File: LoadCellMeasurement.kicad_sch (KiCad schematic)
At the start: 0 parts

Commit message: Add valve control
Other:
- company: (none) -> Queen's Rocket Engineering Team
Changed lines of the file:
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@@
 	(generator_version "9.0")
 	(paper "A4")
+	(title_block
+		(rev "0.1.0")
+		(company "Queen's Rocket Engineering Team")
+	)
 )

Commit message: Add SAFE +24V
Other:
- title: (none) -> Load Cell Measurement
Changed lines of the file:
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@@
 	(paper "A4")
 	(title_block
+		(title "Load Cell Measurement")
 		(rev "0.1.0")
 		(company "Queen's Rocket Engineering Team")

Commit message: Add load cell inputs
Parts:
- added J3: 4-Pin Load Cell, symbol Connector_Generic:Conn_01x04
- added J4: 5-Pin Load Cell, symbol Connector_Generic:Conn_01x05
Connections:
- new net +10V: J4.1 (Pin_1)
- new net +5V: J3.1 (Pin_1)
- new net GND: J3.4 (Pin_4), J4.4 (Pin_4), J4.5 (Pin_5)
- new net LC_FILL_+: J3.2 (Pin_2)
- new net LC_FILL_-: J3.3 (Pin_3)
- new net LC_THRUST_+: J4.2 (Pin_2)
- new net LC_THRUST_-: J4.3 (Pin_3)
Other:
- note added: "Currently this takes up 2 ADC channels per load cell. We could convert this into a single ended reading in the future."

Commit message: v0.1 sch. Add devkit c1 footprint
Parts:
- J3: footprint (none) -> Connector_JST:JST_XH_B4B-XH-A_1x04_P2.50mm_Vertical
- J4: footprint (none) -> Connector_JST:JST_XH_B5B-XH-A_1x05_P2.50mm_Vertical
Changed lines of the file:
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@@
 			)
 		)
-		(property "Footprint" ""
+		(property "Footprint" "Connector_JST:JST_XH_B4B-XH-A_1x04_P2.50mm_Vertical"
 			(at 111.76 85.09 0)
 			(effects
@@
 			)
 		)
-		(property "Footprint" ""
+		(property "Footprint" "Connector_JST:JST_XH_B5B-XH-A_1x05_P2.50mm_Vertical"
 			(at 182.88 87.63 0)
 			(effects

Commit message: routing broken
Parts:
- renumbered J3 to J19, J4 to J20
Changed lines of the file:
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@@
 		(dnp no)
 		(fields_autoplaced yes)
-		(property "Reference" "J3"
+		(property "Reference" "J19"
 			(at 114.3 85.0899 0)
 			(effects
@@
 			(project ""
 				(path "/226c5870-4123-4efa-a2b3-b42d02f59bb7/5c3abfb7-eebf-4fa0-8883-27f893278ab8"
-					(reference "J3")
+					(reference "J19")
 					(unit 1)
 				)
@@
 		(on_board yes)
 		(dnp no)
-		(property "Reference" "#PWR099"
+		(property "Reference" "#PWR095"
 			(at 102.87 97.79 0)
 			(effects
@@
 			(project "nexus"
 				(path "/226c5870-4123-4efa-a2b3-b42d02f59bb7/5c3abfb7-eebf-4fa0-8883-27f893278ab8"
-					(reference "#PWR099")
+					(reference "#PWR095")
 					(unit 1)
 				)
@@
 		(dnp no)
 		(fields_autoplaced yes)
-		(property "Reference" "#PWR098"
+		(property "Reference" "#PWR094"
 			(at 102.87 81.28 0)
 			(effects
@@
 			(project ""
 				(path "/226c5870-4123-4efa-a2b3-b42d02f59bb7/5c3abfb7-eebf-4fa0-8883-27f893278ab8"
-					(reference "#PWR098")
+					(reference "#PWR094")
 					(unit 1)
 				)
@@
 		(on_board yes)
 		(dnp no)
-		(property "Reference" "#PWR096"
+		(property "Reference" "#PWR097"
 			(at 170.18 101.6 0)
 			(effects
@@
 			(project "nexus"
 				(path "/226c5870-4123-4efa-a2b3-b42d02f59bb7/5c3abfb7-eebf-4fa0-8883-27f893278ab8"
-					(reference "#PWR096")
+					(reference "#PWR097")
 					(unit 1)
 				)
@@
 		(dnp no)
 		(fields_autoplaced yes)
-		(property "Reference" "J4"
+		(property "Reference" "J20"
 			(at 185.42 86.3599 0)
 			(effects
@@
 			(project ""
 				(path "/226c5870-4123-4efa-a2b3-b42d02f59bb7/5c3abfb7-eebf-4fa0-8883-27f893278ab8"
-					(reference "J4")
+					(reference "J20")
 					(unit 1)
 				)
@@
 		(dnp no)
 		(fields_autoplaced yes)
-		(property "Reference" "#PWR097"
+		(property "Reference" "#PWR096"
 			(at 170.18 81.28 0)
 			(effects
@@
 			(project ""
 				(path "/226c5870-4123-4efa-a2b3-b42d02f59bb7/5c3abfb7-eebf-4fa0-8883-27f893278ab8"
-					(reference "#PWR097")
-					(unit 1)
-				)
+					(reference "#PWR096")
+					(unit 1)
+				)

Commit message: Fix silk screening
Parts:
- J19, J20: now left out of the parts list
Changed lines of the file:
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@@
 	(title_block
 		(title "Load Cell Measurement")
-		(rev "0.1.0")
+		(rev "1.0.0")
 		(company "Queen's Rocket Engineering Team")
 	)
@@
 		(unit 1)
 		(exclude_from_sim no)
-		(in_bom yes)
+		(in_bom no)
 		(on_board yes)
 		(dnp no)
@@
 		(unit 1)
 		(exclude_from_sim no)
-		(in_bom yes)
+		(in_bom no)
 		(on_board yes)
 		(dnp no)

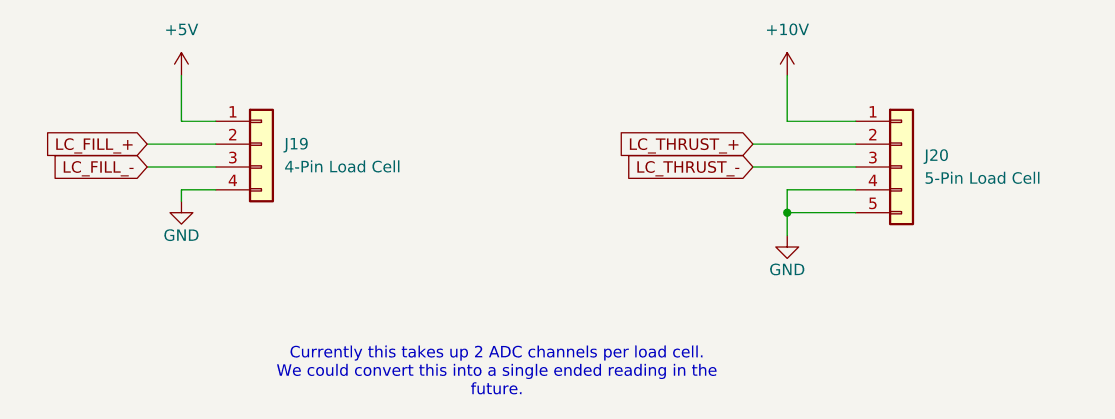
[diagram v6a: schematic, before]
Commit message: Update thrust LC to take +5V. Remove +10V rail
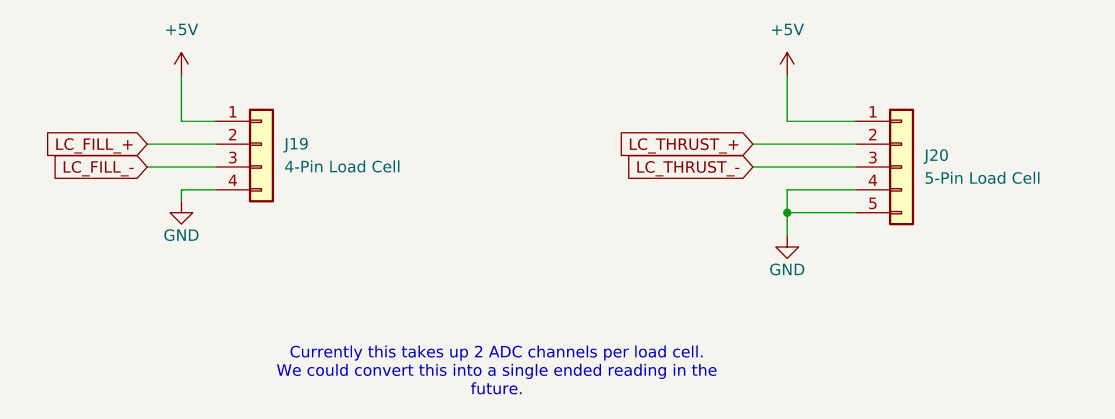
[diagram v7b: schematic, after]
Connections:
- net +10V is gone; now on net +5V: J20.1 (Pin_1)
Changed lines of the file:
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@@
 	)
 	(symbol
-		(lib_id "power:+10V")
+		(lib_id "power:+5V")
 		(at 170.18 77.47 0)
 		(unit 1)
@@
 			)
 		)
-		(property "Value" "+10V"
+		(property "Value" "+5V"
 			(at 170.18 72.39 0)
 			(effects
@@
 			)
 		)
-		(property "Description" "Power symbol creates a global label with name \"+10V\""
+		(property "Description" "Power symbol creates a global label with name \"+5V\""
 			(at 170.18 77.47 0)
 			(effects
@@
 		)
 		(instances
-			(project ""
+			(project "panda"
 				(path "/226c5870-4123-4efa-a2b3-b42d02f59bb7/5c3abfb7-eebf-4fa0-8883-27f893278ab8"
 					(reference "#PWR096")

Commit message: connected to GPIO pins
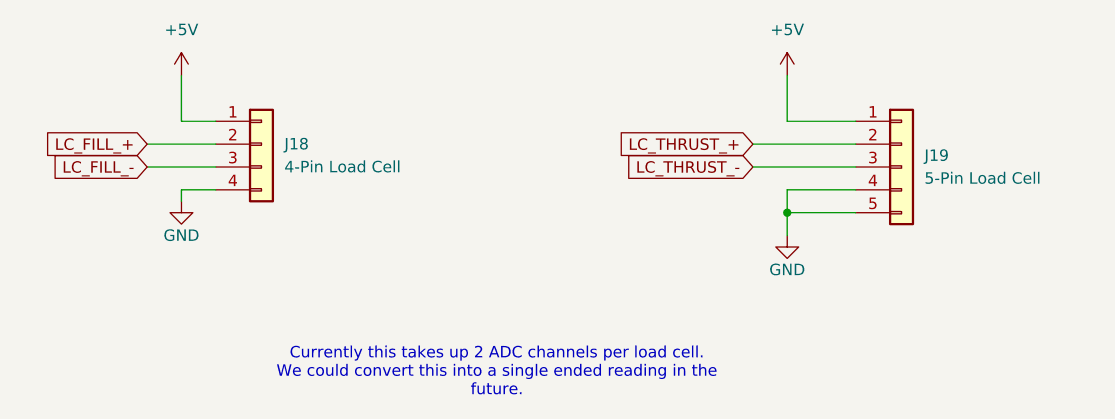
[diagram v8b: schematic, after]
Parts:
- renumbered J19 to J18, J20 to J19
